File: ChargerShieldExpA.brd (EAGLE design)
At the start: 161.3 x 99.1 mm, 58 parts, among them IC1 LM324N, IC2 TL431, Q1 BD648, Q2 BUZ11, Q3 BUZ171, T2 BC548, X1 +5V, X2 Battery, X3 VCC

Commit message: reusable front panel
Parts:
- added LED5, LED6: (no value), bigger:LED5MM_BIG
- added R26, R27: 470, rcl:0207/12
- added S5: A, bigger:TACTILE-PTH-UMSE
- added S6: B, bigger:TACTILE-PTH-UMSE
- S1, S2, S3, S4: device SparkFun-Electromechanical:TACTILE-PTH -> bigger:TACTILE-PTH-UMSE
- moved R1 43.2 mm to (-32.4, 52.1)
- moved LED2 43.2 mm to (-6.35, 74.9)
- moved LED4 43.2 mm to (-15.2, 74.9)
- moved R20 43.2 mm to (-21.6, 67.3)
- moved LED1 43.2 mm to (-6.35, 59.7)
- moved LED3 43.2 mm to (-15.2, 59.7)
- moved R23 43.2 mm to (-21.6, 69.8)
- moved R3 43.2 mm to (-21.6, 64.8)
- moved S3 26.2 mm to (-8.89, 24.1)
- moved S4 23.0 mm to (-26.7, 24.1)
- moved S2 13.7 mm to (-24.1, 6.35)
- moved S1 7.18 mm to (-8.89, 6.35)
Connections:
- new net N$37: S5.3, U$3.6
- new net N$38: S6.3, U$3.7
- new net N$39: LED5.A, R26.2
- new net N$40: LED6.A, R27.2
- new net N$41: R26.1, U$6.6
- new net N$42: R27.1, U$6.7
- net GND2: now also LED5.K, LED6.K, S5.1, S6.1
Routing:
- net N$39: track 0.00 -> 95.8 mm
- net N$37: track 0.00 -> 89.8 mm
- net N$40: track 0.00 -> 73.7 mm
- net N$38: track 0.00 -> 69.3 mm
- net N$22: track 16.6 -> 66.9 mm
- net N$34: track 20.8 -> 64.1 mm
- net N$35: track 52.1 -> 95.3 mm
- net N$33: track 43.0 -> 86.1 mm
- net N$36: track 59.7 -> 102.9 mm
- net N$32: track 23.5 -> 45.4 mm
- net N$4: track 10.1 -> 26.5 mm
- net N$3: track 10.9 -> 24.6 mm
- net N$42: track 0.00 -> 10.7 mm
- net I_SENSE: track 52.8 -> 59.7 mm
- net N$41: track 0.00 -> 6.35 mm
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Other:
- outline, holes or cut-outs redrawn

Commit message: update
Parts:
- moved R6 1.27 mm to (104.1, 38.1)
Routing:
- net N$13: track 102.3 -> 104.3 mm
- net N$7: track 84.9 -> 86.6 mm
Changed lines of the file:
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@@
 <layer number="24" name="bOrigins" color="15" fill="1" visible="yes" active="yes"/>
 <layer number="25" name="tNames" color="7" fill="1" visible="yes" active="yes"/>
-<layer number="26" name="bNames" color="7" fill="1" visible="no" active="yes"/>
-<layer number="27" name="tValues" color="7" fill="1" visible="no" active="yes"/>
-<layer number="28" name="bValues" color="7" fill="1" visible="no" active="yes"/>
+<layer number="26" name="bNames" color="7" fill="1" visible="yes" active="yes"/>
+<layer number="27" name="tValues" color="7" fill="1" visible="yes" active="yes"/>
+<layer number="28" name="bValues" color="7" fill="1" visible="yes" active="yes"/>
 <layer number="29" name="tStop" color="7" fill="3" visible="no" active="yes"/>
 <layer number="30" name="bStop" color="7" fill="6" visible="no" active="yes"/>
@@
 <layer number="37" name="tTest" color="7" fill="1" visible="no" active="yes"/>
 <layer number="38" name="bTest" color="7" fill="1" visible="no" active="yes"/>
-<layer number="39" name="tKeepout" color="4" fill="11" visible="no" active="yes"/>
-<layer number="40" name="bKeepout" color="1" fill="11" visible="no" active="yes"/>
-<layer number="41" name="tRestrict" color="4" fill="10" visible="no" active="yes"/>
-<layer number="42" name="bRestrict" color="1" fill="10" visible="no" active="yes"/>
-<layer number="43" name="vRestrict" color="2" fill="10" visible="no" active="yes"/>
+<layer number="39" name="tKeepout" color="4" fill="11" visible="yes" active="yes"/>
+<layer number="40" name="bKeepout" color="1" fill="11" visible="yes" active="yes"/>
+<layer number="41" name="tRestrict" color="4" fill="10" visible="yes" active="yes"/>
+<layer number="42" name="bRestrict" color="1" fill="10" visible="yes" active="yes"/>
+<layer number="43" name="vRestrict" color="2" fill="10" visible="yes" active="yes"/>
 <layer number="44" name="Drills" color="7" fill="1" visible="no" active="yes"/>
-<layer number="45" name="Holes" color="7" fill="1" visible="yes" active="yes"/>
+<layer number="45" name="Holes" color="7" fill="1" visible="no" active="yes"/>
 <layer number="46" name="Milling" color="3" fill="1" visible="no" active="yes"/>
 <layer number="47" name="Measures" color="7" fill="1" visible="no" active="yes"/>
 <layer number="48" name="Document" color="7" fill="1" visible="no" active="yes"/>
-<layer number="49" name="Reference" color="7" fill="1" visible="no" active="yes"/>
+<layer number="49" name="Reference" color="7" fill="1" visible="yes" active="yes"/>
 <layer number="50" name="dxf" color="7" fill="1" visible="no" active="no"/>
 <layer number="51" name="tDocu" color="7" fill="1" visible="yes" active="yes"/>
-<layer number="52" name="bDocu" color="7" fill="1" visible="no" active="yes"/>
+<layer number="52" name="bDocu" color="7" fill="1" visible="yes" active="yes"/>
 <layer number="53" name="tGND_GNDA" color="7" fill="9" visible="no" active="no"/>
 <layer number="54" name="bGND_GNDA" color="1" fill="9" visible="no" active="no"/>
@@
 <layer number="123" name="tTestmark" color="7" fill="1" visible="no" active="yes"/>
 <layer number="124" name="bTestmark" color="7" fill="1" visible="no" active="yes"/>
-<layer number="125" name="_tNames" color="7" fill="1" visible="no" active="yes"/>
+<layer number="125" name="_tNames" color="7" fill="1" visible="yes" active="yes"/>
 <layer number="126" name="_bNames" color="7" fill="1" visible="no" active="yes"/>
 <layer number="127" name="_tValues" color="7" fill="1" visible="no" active="yes"/>
@@
 <wire x1="2.54" y1="-17.78" x2="2.54" y2="81.28" width="0.1" layer="20"/>
 <dimension x1="-45.72" y1="85.09" x2="114.28" y2="85.09" x3="34.28" y3="87.63" textsize="1.778" layer="47"/>
-<hole x="5.08" y="-15.24" drill="3.2"/>
-<hole x="5.08" y="78.74" drill="3.2"/>
-<hole x="111.76" y="-15.24" drill="3.2"/>
-<hole x="111.76" y="78.74" drill="3.2"/>
+<hole x="7.62" y="-12.7" drill="3.2"/>
+<hole x="7.62" y="76.2" drill="3.2"/>
+<hole x="111.76" y="-12.7" drill="3.2"/>
+<hole x="111.76" y="76.2" drill="3.2"/>
 <wire x1="-45.72" y1="-17.78" x2="-45.72" y2="81.28" width="0.1" layer="20"/>
 <wire x1="-45.72" y1="81.28" x2="1.27" y2="81.28" width="0.1" layer="20"/>
@@
 <element name="R5" library="rcl" package="0207/10" value="1k" x="81.28" y="34.29"/>
 <element name="C3" library="rcl" package="C025_050-025X075" value="15n/60V" x="71.12" y="25.4" rot="R90"/>
-<element name="R6" library="rcl" package="0207/10" value="1k" x="104.14" y="39.37"/>
+<element name="R6" library="rcl" package="0207/10" value="1k" x="104.14" y="38.1"/>
 <element name="Q1" library="transistor-pnp" package="TO220" value="BD648" x="104.14" y="21.59" rot="R180"/>
 <element name="D1" library="diode" package="DO35-7" value="" x="90.17" y="44.45" rot="R90"/>
@@
 <wire x1="85.725" y1="43.18" x2="85.725" y2="35.56" width="0.8128" layer="16"/>
 <wire x1="85.725" y1="35.56" x2="85.725" y2="22.86" width="0.8128" layer="16"/>
-<wire x1="96.52" y1="43.18" x2="85.725" y2="43.18" width="0.8128" layer="16"/>
-<wire x1="96.52" y1="43.18" x2="99.06" y2="39.37" width="0.8128" layer="16"/>
-<wire x1="99.06" y1="39.37" x2="99.06" y2="35.56" width="0.8128" layer="16"/>
+<wire x1="99.06" y1="43.18" x2="85.725" y2="43.18" width="0.8128" layer="16"/>
+<wire x1="99.06" y1="43.18" x2="99.06" y2="38.1" width="0.8128" layer="16"/>
+<wire x1="99.06" y1="38.1" x2="99.06" y2="35.56" width="0.8128" layer="16"/>
 <wire x1="99.06" y1="35.56" x2="106.68" y2="35.56" width="0.8128" layer="16"/>
 <wire x1="106.68" y1="35.56" x2="106.68" y2="27.94" width="0.8128" layer="16"/>
@@
 <contactref element="Q1" pad="3"/>
 <contactref element="X3" pad="1"/>
-<wire x1="105.41" y1="43.18" x2="105.41" y2="39.37" width="1.6764" layer="16"/>
-<wire x1="109.22" y1="39.37" x2="109.22" y2="25.4" width="1.6764" layer="16"/>
+<wire x1="105.41" y1="43.18" x2="105.41" y2="38.1" width="1.6764" layer="16"/>
+<wire x1="109.22" y1="38.1" x2="109.22" y2="25.4" width="1.6764" layer="16"/>
 <wire x1="109.22" y1="25.4" x2="107.95" y2="24.13" width="1.6764" layer="16"/>
 <wire x1="105.41" y1="43.18" x2="105.41" y2="43.22" width="0.6604" layer="16"/>
@@
 <wire x1="104.14" y1="24.13" x2="107.95" y2="24.13" width="1.6764" layer="16"/>
 <wire x1="104.14" y1="20.32" x2="104.14" y2="24.13" width="1.6764" layer="16"/>
-<wire x1="109.22" y1="39.37" x2="105.41" y2="39.37" width="1.6764" layer="16"/>
+<wire x1="109.22" y1="38.1" x2="105.41" y2="38.1" width="1.6764" layer="16"/>
 </signal>
 <signal name="N$9">
@@
 <contactref element="D2" pad="A"/>
 <contactref element="JP1" pad="1"/>
-<wire x1="71.12" y1="24.13" x2="73.66" y2="24.13" width="1.27" layer="16"/>
-<wire x1="73.66" y1="19.05" x2="73.66" y2="15.24" width="1.27" layer="16"/>
-<wire x1="73.66" y1="19.05" x2="73.66" y2="24.13" width="1.27" layer="16"/>
-<wire x1="73.66" y1="24.13" x2="74.93" y2="25.4" width="1.27" layer="16"/>
-<wire x1="74.93" y1="25.4" x2="74.93" y2="29.21" width="1.27" layer="16"/>
+<wire x1="71.12" y1="24.13" x2="73.66" y2="24.13" width="1.6764" layer="16"/>
+<wire x1="73.66" y1="19.05" x2="73.66" y2="15.24" width="1.6764" layer="16"/>
+<wire x1="73.66" y1="19.05" x2="73.66" y2="24.13" width="1.6764" layer="16"/>
+<wire x1="73.66" y1="24.13" x2="74.93" y2="25.4" width="1.6764" layer="16"/>
+<wire x1="74.93" y1="25.4" x2="74.93" y2="29.21" width="1.6764" layer="16"/>
 </signal>
 <signal name="I_SENSE">
@@
 <contactref element="X2" pad="2"/>
 <contactref element="JP2" pad="2"/>
-<wire x1="83.82" y1="15.24" x2="76.2" y2="15.24" width="1.27" layer="16"/>
+<wire x1="83.82" y1="15.24" x2="76.2" y2="15.24" width="1.6764" layer="16"/>
 <wire x1="76.2" y1="19.05" x2="80.01" y2="19.05" width="1.6764" layer="16"/>
 <wire x1="76.2" y1="15.24" x2="76.2" y2="19.05" width="1.6764" layer="16"/>
-<wire x1="83.82" y1="15.24" x2="83.82" y2="19.05" width="1.27" layer="16"/>
+<wire x1="83.82" y1="15.24" x2="83.82" y2="19.05" width="1.6764" layer="16"/>
 <wire x1="80.01" y1="19.05" x2="80.01" y2="44.45" width="1.6764" layer="16"/>
 <wire x1="80.01" y1="44.45" x2="82.51" y2="66.04" width="1.6764" layer="16"/>
 <contactref element="Q2" pad="2"/>
-<wire x1="76.2" y1="15.24" x2="76.2" y2="2.54" width="0.8128" layer="16"/>
-<wire x1="76.2" y1="2.54" x2="81.28" y2="0" width="0.8128" layer="16"/>
-<wire x1="81.28" y1="0" x2="81.28" y2="-10.16" width="0.8128" layer="16"/>
-<wire x1="81.28" y1="-10.16" x2="73.66" y2="-10.16" width="0.8128" layer="16"/>
+<wire x1="76.2" y1="15.24" x2="76.2" y2="0" width="1.6764" layer="16"/>
+<wire x1="76.2" y1="0" x2="81.28" y2="0" width="1.6764" layer="16"/>
+<wire x1="81.28" y1="0" x2="81.28" y2="-10.16" width="1.6764" layer="16"/>
+<wire x1="81.28" y1="-10.16" x2="73.66" y2="-10.16" width="1.6764" layer="16"/>
 </signal>
 <signal name="N$8">

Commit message: front board interconnections
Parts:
- added JP5: (no value), bigger:JP2
- R26, R27: device rcl:0207/12 -> rcl:0204/7
- moved LED2 92.5 mm to (-39.4, -11.4), turned to 180 degrees
- moved LED4 88.2 mm to (-33.0, -11.4), turned to 180 degrees
- moved LED6 86.4 mm to (-3.81, -7.62), turned to 180 degrees
- moved R23 83.8 mm to (-21.6, -14.0), turned to 180 degrees
- moved LED5 81.3 mm to (-11.4, -7.62), turned to 180 degrees
- moved R20 78.7 mm to (-21.6, -11.4), turned to 180 degrees
- moved U$3 74.7 mm to (-33.0, 59.7), turned to 0 degrees
- moved U$6 74.7 mm to (-10.2, 59.7), turned to 180 degrees
- moved R3 73.7 mm to (-21.6, -8.89), turned to 0 degrees
- moved LED1 71.6 mm to (-39.4, -3.81), turned to 180 degrees
- moved LED3 65.9 mm to (-33.0, -3.81), turned to 180 degrees
- moved R26 61.1 mm to (-6.99, 49.5), turned to 0 degrees
- moved R27 56.6 mm to (-6.99, 47.0), turned to 0 degrees
- moved R1 55.2 mm to (-10.8, 1.27), turned to 0 degrees
- moved S1 45.8 mm to (-34.3, 44.5), turned to 270 degrees
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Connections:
- removed net N$22: S3.3, U$3.4
- removed net N$3: S1.3, U$3.2
- removed net N$32: S4.3, U$3.5
- removed net N$33: R3.2, U$6.3
- removed net N$34: R1.2, U$6.2
- removed net N$35: R20.1, U$6.4
- removed net N$36: R23.1, U$6.5
- net +5V: now also JP5.3; no longer C4.1, IC1.4
- net N$1: now also R1.2, U$6.2
- net N$19: now also R3.2, U$6.3
- net N$23: now also S4.3, U$3.5
- net N$26: now also S1.3, U$3.2
- net N$30: now also S2.3, U$3.3
- net N$31: now also S3.3, U$3.4
- net N$37: now also U$4.6
- net N$38: now also U$4.7
- net N$4: now also C4.1, IC1.4, JP5.2; no longer S2.3, U$3.3
- net N$41: now also U$5.6
- net N$42: now also U$5.7
- net PWM_DISCHARGE1: now also R20.1, U$6.4
- net PWM_DISCHARGE2: now also R23.1, U$6.5
- net VCC: now also JP5.1
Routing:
- net N$31: track 9.91 -> 169.5 mm
- net VCC: track 37.4 -> 187.3 mm, vias 0 -> 2
- net N$26: track 16.5 -> 149.0 mm
- net N$23: track 15.7 -> 146.2 mm
- net N$30: track 9.49 -> 136.4 mm
- net PWM_DISCHARGE2: track 74.5 -> 186.8 mm, vias 0 -> 2
- net N$19: track 115.0 -> 224.8 mm
- net PWM_DISCHARGE1: track 63.8 -> 168.5 mm, vias 0 -> 2
- net N$36: track 102.9 -> 0.00 mm
- net N$35: track 95.3 -> 0.00 mm
- net N$33: track 86.1 -> 0.00 mm
- net N$37: track 89.8 -> 167.3 mm
- net N$1: track 24.3 -> 101.7 mm, vias 0 -> 2
- net N$38: track 69.3 -> 139.8 mm
- net N$22: track 66.9 -> 0.00 mm
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
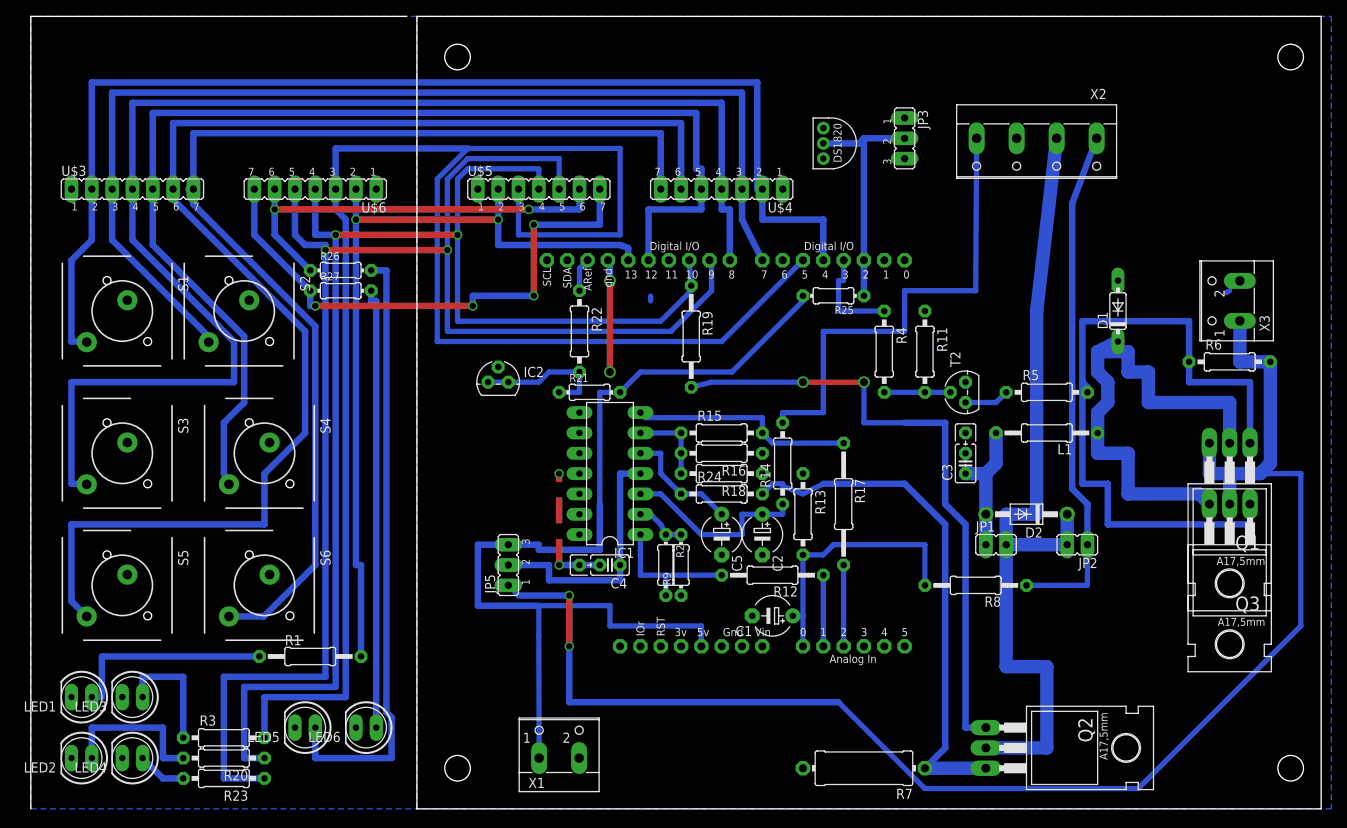
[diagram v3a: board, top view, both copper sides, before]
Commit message: opamp test circuitry
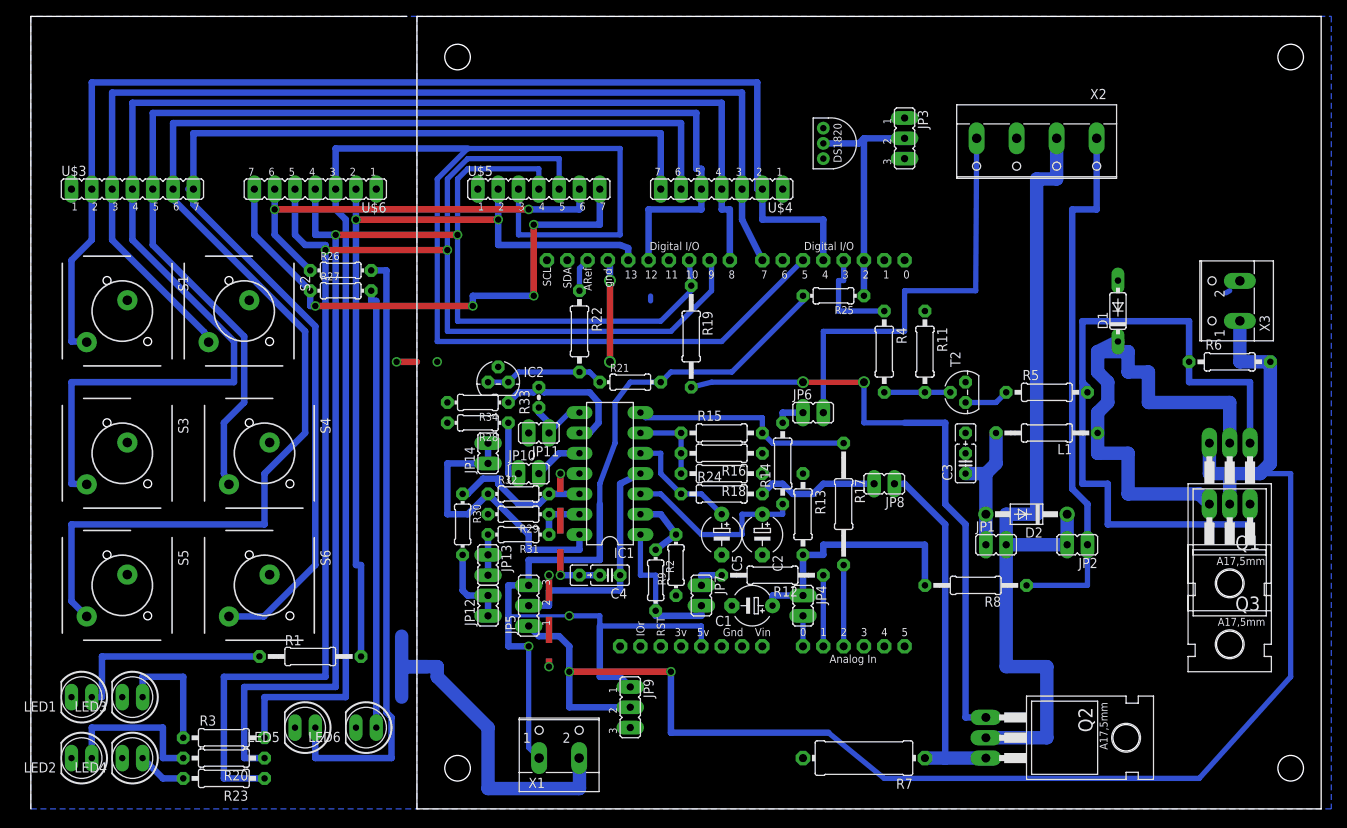
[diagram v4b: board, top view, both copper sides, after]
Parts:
- added JP10, JP11, JP12, JP13, JP14, JP4, JP6, JP7, JP8: (no value), bigger:JP1
- added JP9: (no value), bigger:JP2
- added R28, R29, R30, R31, R32, R34: 0, rcl:0204/7
- added R33: 0, rcl:0204V
- R24: value 1k -> 0
- moved JP5 5.68 mm to (16.5, 7.62)
- moved R21 5.24 mm to (29.2, 35.6)
- moved C1 2.84 mm to (44.5, 7.62)
- moved R2 2.29 mm to (32.4, 10.8)
- moved C4 1.27 mm to (26.7, 11.4)
- moved Q2 1.27 mm to (80.0, -8.89)
- moved R7 1.27 mm to (58.4, -11.4)
- moved R9 0.64 mm to (34.9, 12.7)
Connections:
- new net N$22: JP6.1, R14.2
- new net N$3: C1.+, JP4.1, R13.2, R8.2
- new net N$32: JP7.1, R12.2
- new net N$33: JP8.2, R24.2
- new net N$34: IC1.8, JP11.1, R33.1
- new net N$36: IC1.13, R29.1, R31.1
- new net N$43: IC1.10, JP10.2
- new net N$44: JP10.1, R28.1
- new net N$45: IC1.12, R30.1, R32.2
- new net N$46: JP12.1, JP12.2, R30.2
- new net N$47: JP13.1, JP13.2, R31.2
- new net N$48: IC1.14, JP14.1, JP14.2, R32.1
- new net N$49: IC1.9, R33.2, R34.1
- net +5V: now also JP9.1
- net GND: now also JP9.3, R28.2, R29.2, R34.2
- net I_SENSE: now also JP6.2; no longer R14.2
- net N$11: now also JP7.2; no longer R12.2
- net N$25: now also JP8.1; no longer R24.2
- net U_BATT1: now also JP4.2; no longer C1.+, R13.2, R8.2
- net VCC: now also JP9.2
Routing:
- net GND: track 31.9 -> 80.7 mm, vias 4 -> 7
- net N$48: track 0.00 -> 37.4 mm
- net N$3: track 0.00 -> 31.8 mm
- net U_BATT1: track 33.5 -> 3.81 mm
- net N$25: track 75.6 -> 52.9 mm
- net N$49: track 0.00 -> 18.4 mm
- net N$45: track 0.00 -> 17.6 mm
- net N$33: track 0.00 -> 15.5 mm
- net GND2: track 0.00 -> 13.3 mm, vias 0 -> 1
- net N$46: track 0.00 -> 10.4 mm
- net N$34: track 0.00 -> 8.56 mm
- net N$44: track 0.00 -> 7.62 mm
- net I_SENSE: track 59.7 -> 53.3 mm
- net N$36: track 0.00 -> 6.35 mm
- net N$43: track 0.00 -> 6.13 mm
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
